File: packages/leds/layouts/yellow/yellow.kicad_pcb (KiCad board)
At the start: 2 copper layers, 2 parts, among them U1 2.1V

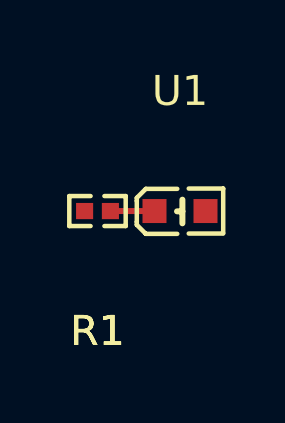
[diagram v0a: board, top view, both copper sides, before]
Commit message: rebuild all packages & regenerate images of changed layouts (silk)
Add new scripts for version bump and build (based on atopile/packages)
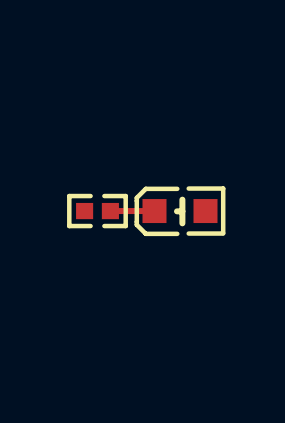
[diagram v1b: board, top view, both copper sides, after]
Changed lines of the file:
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@@
             (at 0 -4 0)
             (layer "F.SilkS")
-            (hide no)
+            (hide yes)
             (effects
                 (font
@@
             )
         )
-        (property "checksum" "0c00a6afa933f634eafebc96eb021e8b94c36af168b29723370c623c9f5e6966"
+        (property "checksum" "f601f7f3d3357b799c6123451ed6dc58c91b2247408d2fb9b234b594b0c11f39"
             (at 0 0 0)
             (layer "User.9")
@@
             )
         )
-        (property "__atopile_lib_fp_hash__" "ff1b765d-fdc4-259d-033c-e6b74928e719"
+        (property "__atopile_lib_fp_hash__" "4bb88092-352a-6cc9-9a65-a84405543f69"
             (at 0 0 0)
             (layer "User.9")
@@
                     (thickness 0.15)
                 )
+                (hide yes)
             )
             (unlocked no)
@@
             (at 0 -4 0)
             (layer "F.SilkS")
-            (hide no)
+            (hide yes)
             (effects
                 (font
@@
                     (thickness 0.15)
                 )
+                (hide yes)
             )
             (unlocked no)
@@
                     (thickness 0.15)
                 )
+                (hide yes)
             )
             (unlocked no)
